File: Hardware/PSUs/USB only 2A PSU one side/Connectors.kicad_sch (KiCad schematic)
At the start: 11 parts, among them J1 Precidip 853-87-004-20-001101, J10 G-Switch-GT-USB-7025, J3 Keystone 3579, J5 Keystone 3569, J7 Keystone 3579, J9 Keystone 3569

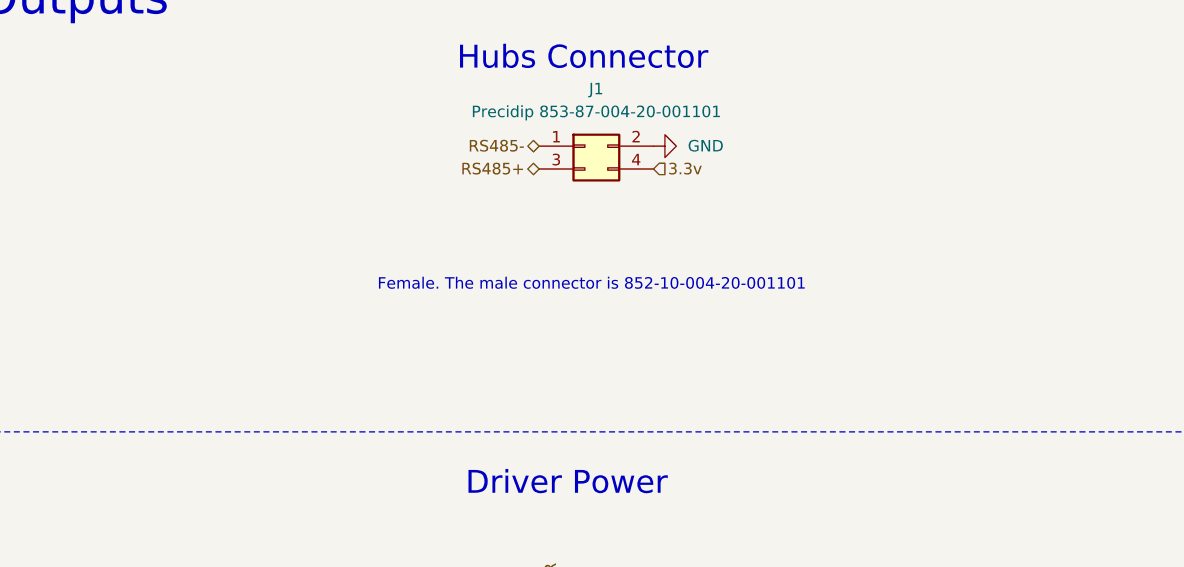
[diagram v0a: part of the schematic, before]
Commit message: Added alt mating connector
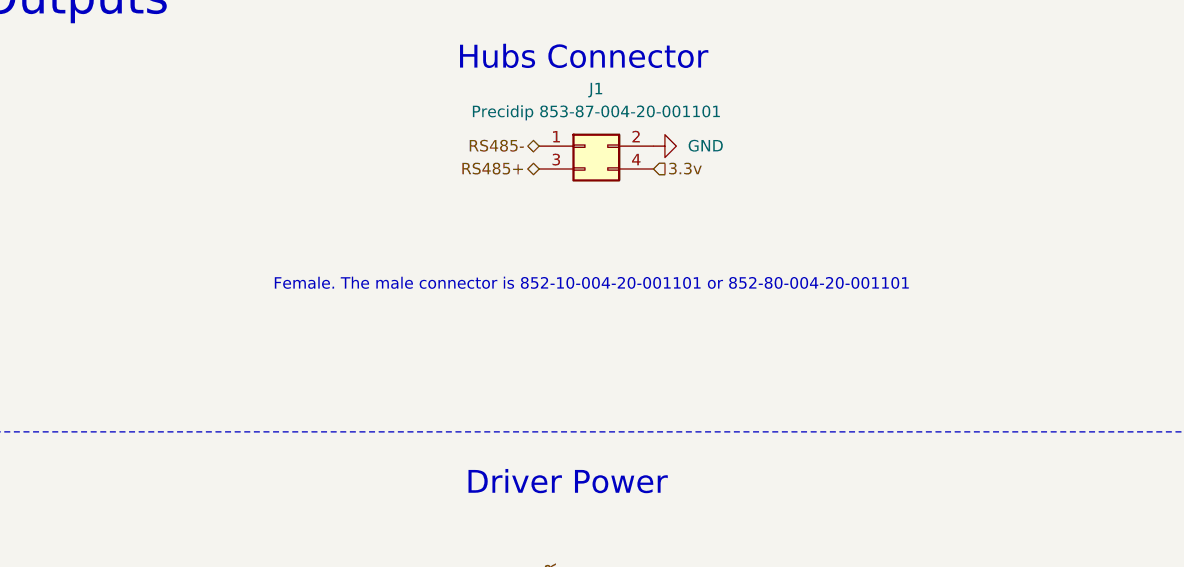
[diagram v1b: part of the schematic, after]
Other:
- note added: "Female. The male connector is 852-10-004-20-001101 or 852-80-004-20-001101"
- note removed: "Female. The male connector is 852-10-004-20-001101"
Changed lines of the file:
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@@
 		(comment 1 "Licensed under CERN-OHL-S")
 	)
-	(text "Female. The male connector is 852-10-004-20-001101"
+	(text "Female. The male connector is 852-10-004-20-001101 or 852-80-004-20-001101"
 		(exclude_from_sim no)
 		(at 206.502 48.514 0)
@@
 		(on_board yes)
 		(dnp no)
-		(property "Reference" "#PWR03"
+		(property "Reference" "#PWR?"
 			(at 88.9 58.42 0)
 			(effects
@@
 				)
 			)
+			(project "Connectors"
+				(path "/ef905b65-82b7-484f-997c-0c6089b83b28"
+					(reference "#PWR?")
+					(unit 1)
+				)
+			)
 		)
 	)
@@
 		(on_board yes)
 		(dnp no)
-		(property "Reference" "#PWR013"
+		(property "Reference" "#PWR?"
 			(at 135.89 64.77 0)
 			(effects
@@
 				)
 			)
+			(project "Connectors"
+				(path "/ef905b65-82b7-484f-997c-0c6089b83b28"
+					(reference "#PWR?")
+					(unit 1)
+				)
+			)
 		)
 	)
@@
 		(dnp no)
 		(fields_autoplaced yes)
-		(property "Reference" "#PWR08"
+		(property "Reference" "#PWR?"
 			(at 201.93 118.11 0)
 			(effects
@@
 				)
 			)
+			(project "Connectors"
+				(path "/ef905b65-82b7-484f-997c-0c6089b83b28"
+					(reference "#PWR?")
+					(unit 1)
+				)
+			)
 		)
 	)
@@
 		(dnp no)
 		(fields_autoplaced yes)
-		(property "Reference" "#FLG01"
+		(property "Reference" "#FLG?"
 			(at 76.2 42.545 0)
 			(effects
@@
 		(on_board yes)
 		(dnp no)
-		(property "Reference" "R2"
+		(property "Reference" "R?"
 			(at 86.614 39.37 0)
 			(effects
@@
 				)
 			)
+			(project "Connectors"
+				(path "/ef905b65-82b7-484f-997c-0c6089b83b28"
+					(reference "R?")
+					(unit 1)
+				)
+			)
 		)
 	)
@@
 		(on_board yes)
 		(dnp yes)
-		(property "Reference" "J7"
+		(property "Reference" "J?"
 			(at 205.232 105.664 0)
 			(effects
@@
 		(on_board yes)
 		(dnp yes)
-		(property "Reference" "J3"
+		(property "Reference" "J?"
 			(at 205.232 95.504 0)
 			(effects
@@
 		(dnp no)
 		(fields_autoplaced yes)
-		(property "Reference" "#PWR028"
+		(property "Reference" "#PWR?"
 			(at 219.71 33.02 0)
 			(effects
@@
 		(on_board yes)
 		(dnp no)
-		(property "Reference" "C7"
+		(property "Reference" "C?"
 			(at 84.836 46.228 0)
 			(effects
@@
 				)
 			)
+			(project "Connectors"
+				(path "/ef905b65-82b7-484f-997c-0c6089b83b28"
+					(reference "C?")
+					(unit 1)
+				)
+			)
 		)
 	)
@@
 		(dnp no)
 		(fields_autoplaced yes)
-		(property "Reference" "J1"
+		(property "Reference" "J?"
 			(at 207.01 26.67 0)
 			(effects
@@
 				)
 			)
+			(project "Connectors"
+				(path "/ef905b65-82b7-484f-997c-0c6089b83b28"
+					(reference "J?")
+					(unit 1)
+				)
+			)
 		)
 	)
@@
 		(on_board yes)
 		(dnp no)
-		(property "Reference" "R19"
+		(property "Reference" "R?"
 			(at 117.348 57.912 0)
 			(effects
@@
 				)
 			)
+			(project "Connectors"
+				(path "/ef905b65-82b7-484f-997c-0c6089b83b28"
+					(reference "R?")
+					(unit 1)
+				)
+			)
 		)
 	)
@@
 		(on_board yes)
 		(dnp yes)
-		(property "Reference" "J5"
+		(property "Reference" "J?"
 			(at 203.962 98.552 0)
 			(effects
@@
 		(on_board yes)
 		(dnp no)
-		(property "Reference" "D11"
+		(property "Reference" "D?"
 			(at 94.234 73.406 0)
 			(effects
@@
 				)
 			)
+			(project "Connectors"
+				(path "/ef905b65-82b7-484f-997c-0c6089b83b28"
+					(reference "D?")
+					(unit 1)
+				)
+			)
 		)
 	)
@@
 		(dnp no)
 		(fields_autoplaced yes)
-		(property "Reference" "J10"
+		(property "Reference" "J?"
 			(at 52.07 44.45 0)
 			(effects
@@
 				(path "/eb3f183d-8bb1-43a5-a363-092ed67891e3/3a3003bc-8e40-4cd7-b859-421f37e4b48c"
 					(reference "J10")
+					(unit 1)
+				)
+			)
+			(project "Connectors"
+				(path "/ef905b65-82b7-484f-997c-0c6089b83b28"
+					(reference "J?")
 					(unit 1)
 				)
@@
 		(on_board yes)
 		(dnp no)
-		(property "Reference" "R33"
+		(property "Reference" "R?"
 			(at 123.698 56.896 0)
 			(effects
@@
 				)
 			)
+			(project "Connectors"
+				(path "/ef905b65-82b7-484f-997c-0c6089b83b28"
+					(reference "R?")
+					(unit 1)
+				)
+			)
 		)
 	)
@@
 		(on_board yes)
 		(dnp yes)
-		(property "Reference" "J9"
+		(property "Reference" "J?"
 			(at 203.962 108.712 0)
 			(effects
@@
 		(dnp no)
 		(fields_autoplaced yes)
-		(property "Reference" "#PWR02"
+		(property "Reference" "#PWR?"
 			(at 48.26 97.79 0)
 			(effects
@@
 					(unit 1)
 				)
+			)
+			(project "Connectors"
+				(path "/ef905b65-82b7-484f-997c-0c6089b83b28"
+					(reference "#PWR?")
+					(unit 1)
+				)
